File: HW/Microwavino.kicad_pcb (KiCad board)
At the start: 2 copper layers, 57 parts, among them P1 SMA, P2 SMA, P3 SMA, P4 SMA, U1 MIC5366, U2 MCP1824T, U3 MCP1824T, U4 MCP1824T, U5 ASTXR-12-19.200MHz, U6 MAX2871, U7 Teensy3.2

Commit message: prelim layout
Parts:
- removed C27, C29, C30: 1n, VNA:C_0603b
- removed P2, P3, P4: SMA, VNA:CONSMA003.062
- removed R10: 49.9, VNA:R_0402b
- added R13: DNP, VNA:R_0402b, F.Cu at (219.7, 79.4)
- added R14: DNP, VNA:R_0402b, F.Cu at (227.5, 79.4)
- C26: footprint VNA:C_0603b -> VNA:C_0402b
- U1: footprint VNA:SOT-23-5L -> VNA:SOT-23-5
- moved U7 100.8 mm to (89.5, 69.8), turned to 270 degrees
- moved C28 58.6 mm to (171.3, 76.2)
- moved R9 58.6 mm to (169.4, 75.6)
- moved R11 54.2 mm to (151.8, 75.6)
- moved C25 50.6 mm to (138.3, 76.2)
- moved R6 50.6 mm to (136.4, 75.6)
- moved R7 50.6 mm to (136.4, 76.8)
- moved P1 23.2 mm to (89.7, 85.5)
- moved C26 19.8 mm to (89.7, 81.5)
- moved R8 19.0 mm to (91.4, 80.7), turned to 180 degrees
- moved C1 11.4 mm to (85.7, 59.4), turned to 180 degrees
- moved U1 8.87 mm to (86.6, 60.8), turned to 180 degrees
- moved C5 3.16 mm to (85.7, 65.0), turned to 180 degrees
- moved R3 1.94 mm to (83.4, 75.6), turned to 270 degrees
- moved R12 1.45 mm to (85.5, 72.9), turned to 0 degrees
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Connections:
- FB3 pad 2: Net-(FB3-Pad2) -> /3V3_PLL
- U7 pad 6: CE -> LE
- U7 pad 7: LE -> CE
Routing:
- net Net-(C24-Pad1): track 0.00 -> 16.6 mm, vias 0 -> 2
- net DATA: track 0.00 -> 14.9 mm, vias 0 -> 1
- net RFOUT_EN: track 0.00 -> 12.4 mm, vias 0 -> 1
- net LE: track 0.00 -> 11.6 mm
- net CE: track 0.00 -> 10.1 mm
- net MUXOUT: track 0.00 -> 9.60 mm, vias 0 -> 1
- net Net-(R3-Pad2): track 0.00 -> 7.42 mm, vias 0 -> 2
- net /3V3_PLL: track 0.00 -> 5.86 mm
- net /3V3_DIG: track 0.00 -> 5.81 mm
- net /3V3_VCO: track 0.00 -> 5.29 mm
- net /RF_OUTA_P: track 0.00 -> 4.37 mm
- net Net-(C12-Pad1): track 0.00 -> 3.36 mm
- net Net-(C26-Pad1): track 0.00 -> 3.27 mm
- net /RF_OUTB_N: track 0.00 -> 3.11 mm
- net Net-(C9-Pad1): track 0.00 -> 2.91 mm
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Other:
- board outline added: 17.8 x 35.6 mm
- net class Default: clearance 0.2 -> 0.1524; via_dia 0.6 -> 0.554; via_drill 0.4 -> 0.3
- net class PWR: clearance 0.1 -> 0.1524; via_dia 0.4 -> 0.554
- net class RF: clearance 0.1 -> 0.2; trace_width 0.75 -> 0.85; via_dia 0.4 -> 0.554
- net class SPI: clearance 0.1 -> 0.1524; via_dia 0.4 -> 0.554
- rule trace_clearance: 0.2 -> 0.1524

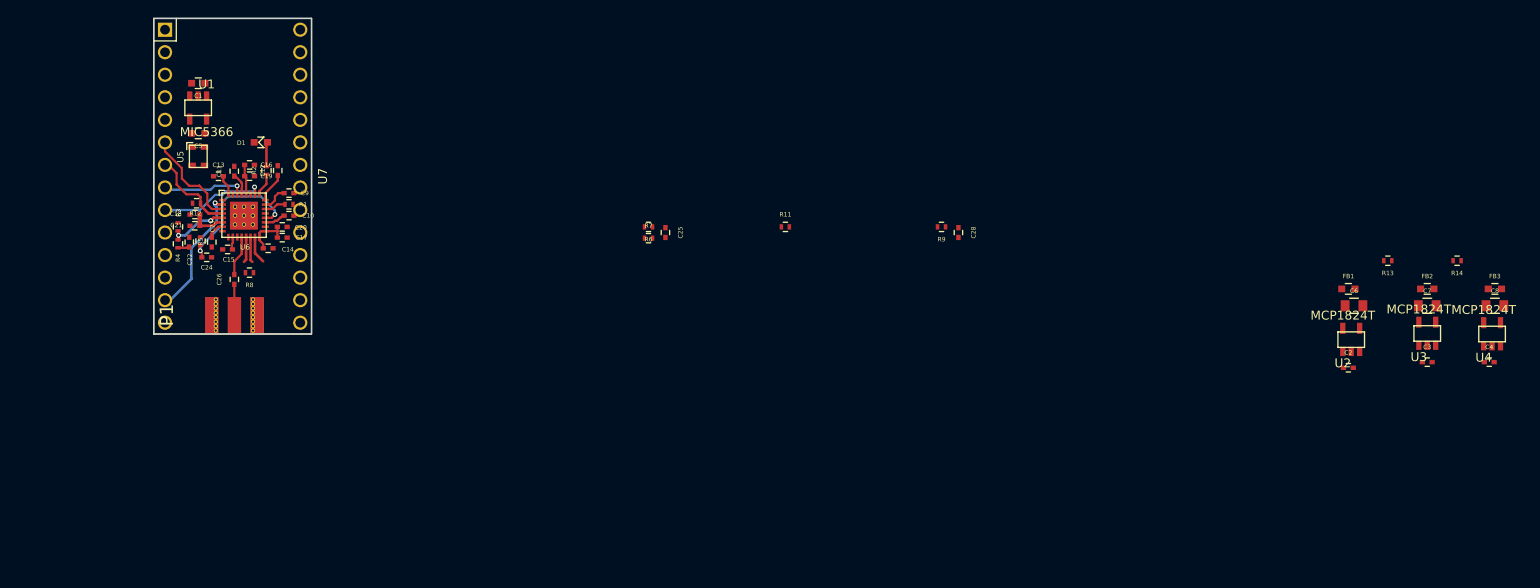
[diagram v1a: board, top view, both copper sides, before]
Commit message: route all except power
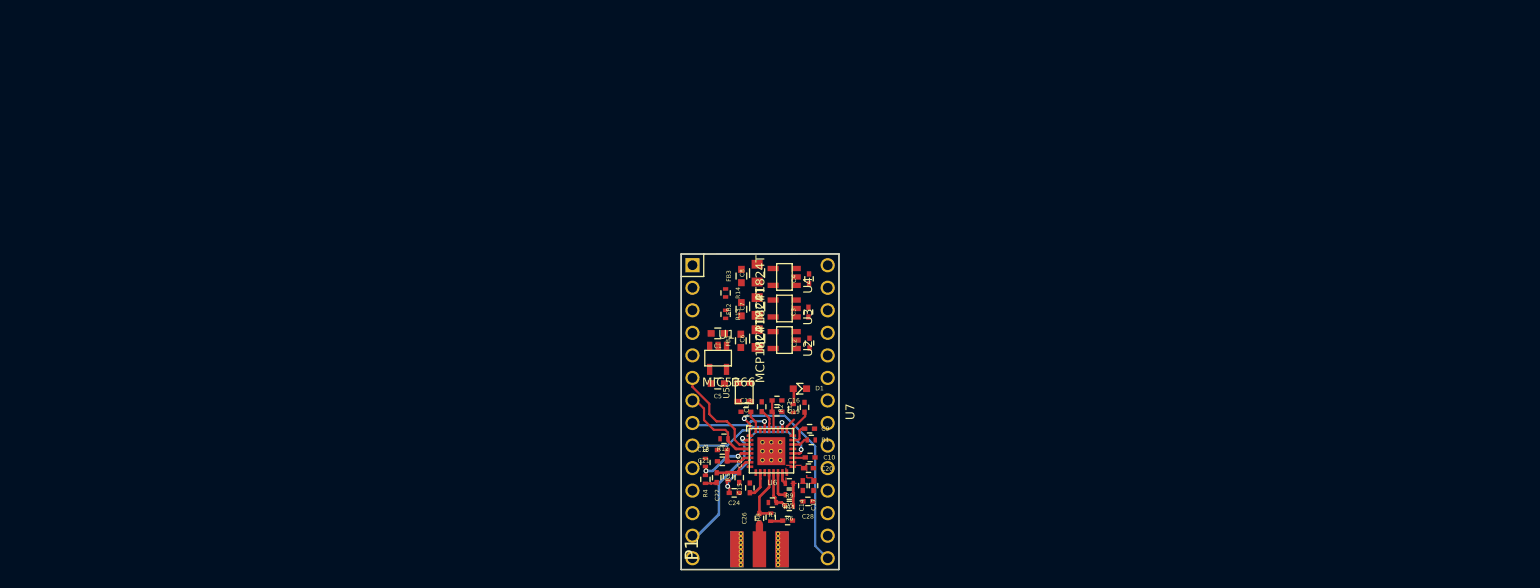
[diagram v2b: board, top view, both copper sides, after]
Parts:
- moved FB3 84.9 mm to (146.9, 81.1), turned to 90 degrees
- moved C8 83.2 mm to (148.6, 80.8), turned to 90 degrees
- moved R14 82.5 mm to (145.1, 83.0), turned to 270 degrees
- moved U4 79.1 mm to (151.8, 81.2), turned to 180 degrees
- moved FB2 77.3 mm to (146.9, 84.8), turned to 90 degrees
- moved C4 77.2 mm to (154.5, 81.4), turned to 90 degrees
- moved C7 75.5 mm to (148.7, 84.5), turned to 90 degrees
- moved R13 74.9 mm to (145.1, 85.4), turned to 270 degrees
- moved U3 71.6 mm to (151.8, 84.7), turned to 180 degrees
- moved C3 70.0 mm to (154.4, 85.2), turned to 90 degrees
- moved FB1 68.7 mm to (146.8, 88.4), turned to 90 degrees
- moved C6 67.4 mm to (148.7, 88.1), turned to 90 degrees
- moved U5 67.0 mm to (147.2, 94.2)
- moved D1 66.8 mm to (153.5, 93.8), turned to 180 degrees
- moved C17 66.1 mm to (155.0, 104.7), turned to 270 degrees
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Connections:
- U7 pad 33: Net-(U7-Pad33) -> VCC
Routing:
- net CLK: track 0.00 -> 25.0 mm, vias 0 -> 1
- net Net-(C22-Pad2): track 2.05 -> 5.65 mm
- net /3V3_PLL: track 5.86 -> 8.18 mm
- net /RF_OUTA_P: track 4.37 -> 6.34 mm
- net /RF_OUTA_N: track 2.90 -> 4.67 mm
- net /RF_OUTB_N: track 3.11 -> 1.35 mm
- net /3V3_VCO: track 5.29 -> 3.92 mm
- net Net-(D1-Pad2): track 2.77 -> 1.54 mm
- net LD: track 2.54 -> 1.47 mm
- net Net-(C10-Pad1): track 2.43 -> 1.42 mm
- net Net-(R1-Pad1): track 2.43 -> 1.92 mm
- added copper zone on F.Cu, net /3V3_VCO

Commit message: layout completed v1.0
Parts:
- added REF**: Via_0.3_0.6, VNA:Via_0.3_0.6, F.Cu at (147.8, 109.3)
- added REF**: Via_0.3_0.6, VNA:Via_0.3_0.6, F.Cu at (144.2, 90.8)
- added REF**: Via_0.3_0.6, VNA:Via_0.3_0.6, F.Cu at (144.3, 89.0)
- added REF**: Via_0.3_0.6, VNA:Via_0.3_0.6, F.Cu at (144.5, 101.5)
- added REF**: Via_0.3_0.6, VNA:Via_0.3_0.6, F.Cu at (142.9, 100.2)
- added REF**: Via_0.3_0.6, VNA:Via_0.3_0.6, F.Cu at (148.2, 103.8)
- added REF**: Via_0.3_0.6, VNA:Via_0.3_0.6, F.Cu at (147.6, 106.2)
- added REF**: Via_0.3_0.6, VNA:Via_0.3_0.6, F.Cu at (146.7, 106.6)
- added REF**: Via_0.3_0.6, VNA:Via_0.3_0.6, F.Cu at (149.9, 106.1)
- added REF**: Via_0.3_0.6, VNA:Via_0.3_0.6, F.Cu at (152.6, 109.5)
- added REF**: Via_0.3_0.6, VNA:Via_0.3_0.6, F.Cu at (152.4, 90.6)
- added REF**: Via_0.3_0.6, VNA:Via_0.3_0.6, F.Cu at (148.1, 106.7)
- added REF**: Via_0.3_0.6, VNA:Via_0.3_0.6, F.Cu at (151.8, 88.3)
- added REF**: Via_0.3_0.6, VNA:Via_0.3_0.6, F.Cu at (151.8, 81.2)
- added REF**: Via_0.3_0.6, VNA:Via_0.3_0.6, F.Cu at (151.8, 84.8)
- added REF**: Via_0.3_0.6, VNA:Via_0.3_0.6, F.Cu at (151.8, 83.2)
- added REF**: Via_0.3_0.6, VNA:Via_0.3_0.6, F.Cu at (151.8, 86.5)
- added REF**: Via_0.3_0.6, VNA:Via_0.3_0.6, F.Cu at (143.9, 80.5)
- added REF**: Via_0.3_0.6, VNA:Via_0.3_0.6, F.Cu at (143.6, 86.1)
- added REF**: Via_0.3_0.6, VNA:Via_0.3_0.6, F.Cu at (148.1, 107.4)
- added REF**: Via_0.3_0.6, VNA:Via_0.3_0.6, F.Cu at (148.1, 108.4)
- added REF**: Via_0.3_0.6, VNA:Via_0.3_0.6, F.Cu at (149.9, 109.3)
- added REF**: Via_0.3_0.6, VNA:Via_0.3_0.6, F.Cu at (150.2, 107.4)
- added REF**: Via_0.3_0.6, VNA:Via_0.3_0.6, F.Cu at (145.9, 96.4)
- added REF**: Via_0.3_0.6, VNA:Via_0.3_0.6, F.Cu at (145.5, 95.2)
- added REF**: Via_0.3_0.6, VNA:Via_0.3_0.6, F.Cu at (143.4, 94.2)
- moved C15 0.81 mm to (148.4, 104.4), turned to 180 degrees
- moved C25 0.60 mm to (152.6, 108.3)
- moved R12 0.52 mm to (144.8, 98.9)
- moved R8 0.32 mm to (150.5, 108.3), turned to 180 degrees
- moved C24 0.09 mm to (146.1, 105.6)
- turned C28 to 0 degrees
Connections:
- D1 pad 2: Net-(D1-Pad2) -> LD
- R12 pad 1: /3V3_DIG -> /3V3_PLL
- R2 pad 1: LD -> Net-(R2-Pad1)
- R2 pad 2: Net-(D1-Pad2) -> LD
- U6 pad 25: LD -> Net-(R2-Pad1)
- U7 pad 10: LD -> Net-(U7-Pad10)
- U7 pad 28: Net-(U7-Pad28) -> LD
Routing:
- net GND: track 0.00 -> 42.2 mm
- net /3V3_PLL: track 8.18 -> 39.6 mm, vias 0 -> 4
- net /3V3_VCO: track 3.92 -> 33.0 mm, vias 0 -> 2
- net /3V3_DIG: track 5.81 -> 19.5 mm, vias 0 -> 3
- net /3V3_IN: track 0.00 -> 12.4 mm
- net Net-(C7-Pad1): track 0.00 -> 7.23 mm
- net /1V8: track 0.00 -> 5.43 mm
- net LD: track 1.47 -> 6.38 mm
- net Net-(C8-Pad1): track 0.00 -> 3.62 mm
- net Net-(R2-Pad1): track 0.00 -> 2.47 mm
- net Net-(D1-Pad2): track 1.54 -> 0.00 mm
- net /CLK_REF: track 0.00 -> 1.28 mm
- net DATA: track 14.9 -> 16.1 mm
- net Net-(R3-Pad2): track 7.42 -> 8.49 mm
- net CE: track 10.1 -> 11.1 mm
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- added copper zone on B.Cu, net GND
- added copper zone on F.Cu, net GND
- added copper zone on F.Cu, net VCC
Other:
- board text added: "More things I hate about Kicad: - When I set Front layer to invisible, I want to hide all of Front layer, and not leave pads visible! - When I reroute the trace, I want old trace deleted every time, not leave it standing there as it was or delete it only sometimes. - For via stitching I need to create component pads - Duplicate component works only in F11 view"

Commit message: drc pass
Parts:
- removed the REF** at (147.8, 109.3)
- removed the REF** at (144.2, 90.8)
- removed the REF** at (144.3, 89.0)
- removed the REF** at (144.5, 101.5)
- removed the REF** at (142.9, 100.2)
- removed the REF** at (148.2, 103.8)
- removed the REF** at (147.6, 106.2)
- removed the REF** at (146.7, 106.6)
- removed the REF** at (149.9, 106.1)
- removed the REF** at (152.6, 109.5)
- removed the REF** at (152.4, 90.6)
- removed the REF** at (148.1, 106.7)
- removed the REF** at (151.8, 88.3)
- removed the REF** at (151.8, 81.2)
- removed the REF** at (151.8, 83.2)
- removed the REF** at (151.8, 86.5)
- removed the REF** at (143.9, 80.5)
- removed the REF** at (143.6, 86.1)
- removed the REF** at (148.1, 107.4)
- removed the REF** at (148.1, 108.4)
- removed the REF** at (150.2, 107.4)
- removed the REF** at (145.9, 96.4)
- removed the REF** at (145.5, 95.2)
- removed the REF** at (143.4, 94.2)
- added REF**: Via_0.3_0.6, VNA:Via_0.3_0.6, F.Cu at (144.2, 91.6)
- added REF**: Via_0.3_0.6, VNA:Via_0.3_0.6, F.Cu at (154.7, 112.2)
- added REF**: Via_0.3_0.6, VNA:Via_0.3_0.6, F.Cu at (154.4, 108.2)
- added REF**: Via_0.3_0.6, VNA:Via_0.3_0.6, F.Cu at (154.4, 109.5)
- added REF**: Via_0.3_0.6, VNA:Via_0.3_0.6, F.Cu at (155.2, 110.3)
- added REF**: Via_0.3_0.6, VNA:Via_0.3_0.6, F.Cu at (155.1, 113.4)
- added REF**: Via_0.3_0.6, VNA:Via_0.3_0.6, F.Cu at (155.1, 97.7)
- added REF**: Via_0.3_0.6, VNA:Via_0.3_0.6, F.Cu at (154.9, 107.2)
- added REF**: Via_0.3_0.6, VNA:Via_0.3_0.6, F.Cu at (155.7, 106.5)
- added REF**: Via_0.3_0.6, VNA:Via_0.3_0.6, F.Cu at (144.1, 108.5)
- added REF**: Via_0.3_0.6, VNA:Via_0.3_0.6, F.Cu at (144.1, 111.4)
- added REF**: Via_0.3_0.6, VNA:Via_0.3_0.6, F.Cu at (152.9, 113.5)
- added REF**: Via_0.3_0.6, VNA:Via_0.3_0.6, F.Cu at (145.3, 113.4)
- added REF**: Via_0.3_0.6, VNA:Via_0.3_0.6, F.Cu at (144.1, 113.4)
- added REF**: Via_0.3_0.6, VNA:Via_0.3_0.6, F.Cu at (142.9, 113.4)
- added REF**: Via_0.3_0.6, VNA:Via_0.3_0.6, F.Cu at (144.2, 105.5)
- added REF**: Via_0.3_0.6, VNA:Via_0.3_0.6, F.Cu at (142.5, 98.7)
- added REF**: Via_0.3_0.6, VNA:Via_0.3_0.6, F.Cu at (142.9, 100.2)
- added REF**: Via_0.3_0.6, VNA:Via_0.3_0.6, F.Cu at (151.1, 107.5)
- added REF**: Via_0.3_0.6, VNA:Via_0.3_0.6, F.Cu at (151.5, 109.2)
- added REF**: Via_0.3_0.6, VNA:Via_0.3_0.6, F.Cu at (147.9, 109.3)
- added REF**: Via_0.3_0.6, VNA:Via_0.3_0.6, F.Cu at (155.6, 91.2)
- added REF**: Via_0.3_0.6, VNA:Via_0.3_0.6, F.Cu at (148.1, 108.4)
- added REF**: Via_0.3_0.6, VNA:Via_0.3_0.6, F.Cu at (148.2, 107.2)
- added REF**: Via_0.3_0.6, VNA:Via_0.3_0.6, F.Cu at (148.2, 106.2)
- added REF**: Via_0.3_0.6, VNA:Via_0.3_0.6, F.Cu at (147.8, 103.1)
- added REF**: Via_0.3_0.6, VNA:Via_0.3_0.6, F.Cu at (147.8, 103.8)
- added REF**: Via_0.3_0.6, VNA:Via_0.3_0.6, F.Cu at (147.2, 104.4)
- added REF**: Via_0.3_0.6, VNA:Via_0.3_0.6, F.Cu at (146.7, 106.2)
- added REF**: Via_0.3_0.6, VNA:Via_0.3_0.6, F.Cu at (146.2, 98.4)
- added REF**: Via_0.3_0.6, VNA:Via_0.3_0.6, F.Cu at (143.9, 102.4)
- added REF**: Via_0.3_0.6, VNA:Via_0.3_0.6, F.Cu at (145.6, 95.2)
- added REF**: Via_0.3_0.6, VNA:Via_0.3_0.6, F.Cu at (145.9, 84.3)
- added REF**: Via_0.3_0.6, VNA:Via_0.3_0.6, F.Cu at (143.5, 94.3)
- added REF**: Via_0.3_0.6, VNA:Via_0.3_0.6, F.Cu at (143.8, 86.2)
- added REF**: Via_0.3_0.6, VNA:Via_0.3_0.6, F.Cu at (143.8, 84.5)
- added REF**: Via_0.3_0.6, VNA:Via_0.3_0.6, F.Cu at (144.4, 81.0)
- added REF**: Via_0.3_0.6, VNA:Via_0.3_0.6, F.Cu at (142.9, 82.4)
- added REF**: Via_0.3_0.6, VNA:Via_0.3_0.6, F.Cu at (145.9, 79.4)
- added REF**: Via_0.3_0.6, VNA:Via_0.3_0.6, F.Cu at (151.2, 79.3)
- added REF**: Via_0.3_0.6, VNA:Via_0.3_0.6, F.Cu at (152.1, 90.1)
- added REF**: Via_0.3_0.6, VNA:Via_0.3_0.6, F.Cu at (151.8, 88.3)
- added REF**: Via_0.3_0.6, VNA:Via_0.3_0.6, F.Cu at (151.8, 86.6)
- added REF**: Via_0.3_0.6, VNA:Via_0.3_0.6, F.Cu at (146.0, 82.6)
- added REF**: Via_0.3_0.6, VNA:Via_0.3_0.6, F.Cu at (151.8, 83.1)
- added REF**: Via_0.3_0.6, VNA:Via_0.3_0.6, F.Cu at (151.8, 81.2)
- added REF**: Via_0.3_0.6, VNA:Via_0.3_0.6, F.Cu at (154.8, 95.4)
- added REF**: Via_0.3_0.6, VNA:Via_0.3_0.6, F.Cu at (155.1, 93.9)
- added REF**: Via_0.3_0.6, VNA:Via_0.3_0.6, F.Cu at (152.8, 109.1)
- added REF**: Via_0.3_0.6, VNA:Via_0.3_0.6, F.Cu at (149.9, 107.2)
- added REF**: Via_0.3_0.6, VNA:Via_0.3_0.6, F.Cu at (145.9, 96.4)
- added REF**: Via_0.3_0.6, VNA:Via_0.3_0.6, F.Cu at (146.5, 94.4)
- added REF**: Via_0.3_0.6, VNA:Via_0.3_0.6, F.Cu at (152.8, 110.3)
- added REF**: Via_0.3_0.6, VNA:Via_0.3_0.6, F.Cu at (153.7, 111.1)
- moved R12 0.29 mm to (144.5, 98.9)
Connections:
- U7 pad 10: Net-(U7-Pad10) -> GND
- U7 pad 11: Net-(U7-Pad11) -> GND
- U7 pad 14: Net-(U7-Pad14) -> MUXOUT
- U7 pad 23: Net-(U7-Pad23) -> GND
- U7 pad 24: Net-(U7-Pad24) -> GND
- U7 pad 8: MUXOUT -> RFOUT_EN
- U7 pad 9: RFOUT_EN -> Net-(U7-Pad9)
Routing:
- net MUXOUT: track 9.60 -> 20.6 mm
- net Net-(C8-Pad1): track 3.62 -> 5.42 mm
- net /3V3_PLL: track 39.6 -> 40.9 mm
- net CE: track 11.1 -> 10.5 mm
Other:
- board text added: "More things I hate about Kicad: - When I set Front layer to invisible, I want to hide all of Front layer, and not leave pads visible! - When I reroute the trace, I want old trace deleted every time, not leave it standing there as it was or delete it only sometimes. - For via stitching I need to create component pads - and then, reading new netlist kills those pads - Duplicate component works only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"
- board text removed: "More things I hate about Kicad: - When I set Front layer to invisible, I want to hide all of Front layer, and not leave pads visible! - When I reroute the trace, I want old trace deleted every time, not leave it standing there as it was or delete it only sometimes. - For via stitching I need to create component pads - Duplicate component works only in F11 view"

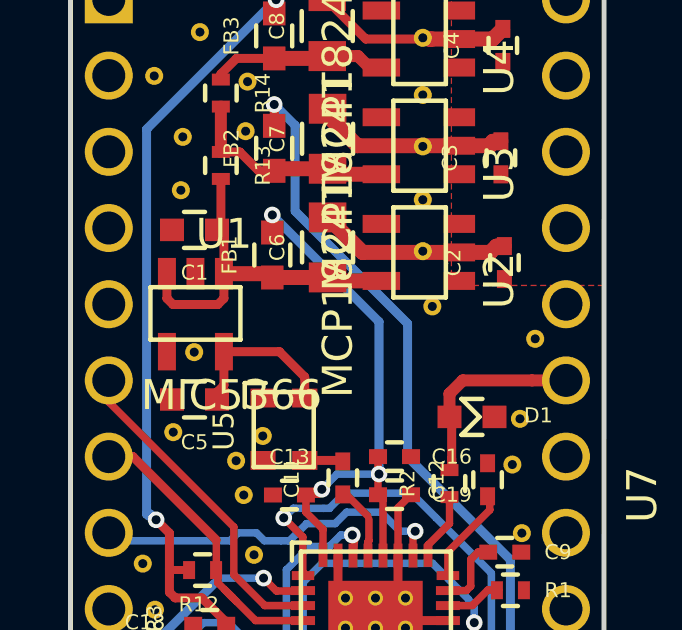
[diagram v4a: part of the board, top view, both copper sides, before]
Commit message: added footprint SOT-323-70-sc-5
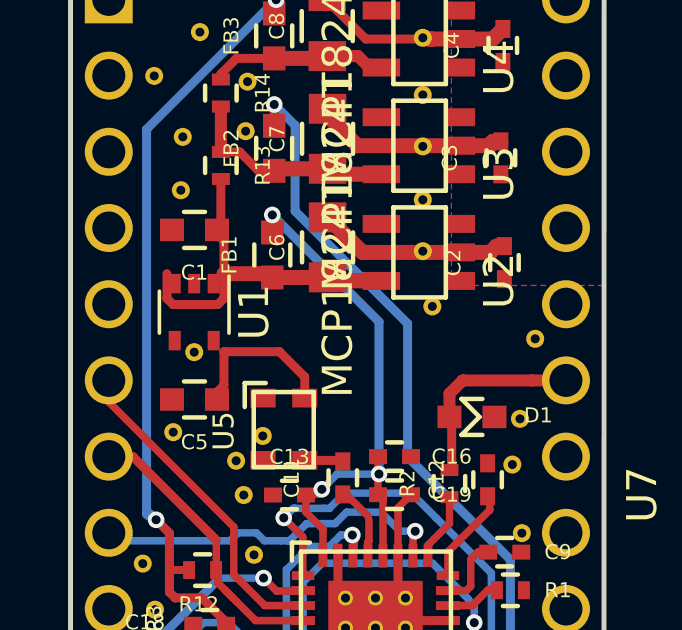
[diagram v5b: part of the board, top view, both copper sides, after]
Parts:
- U1: footprint VNA:SOT-23-5 -> VNA:SOT-353_SC-70-5
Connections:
- U2 pad 4: Net-(U2-Pad4) -> (no net)
- U3 pad 4: Net-(U3-Pad4) -> (no net)
- U4 pad 4: Net-(U4-Pad4) -> (no net)
- U7 pad 12: Net-(U7-Pad12) -> (no net)
- U7 pad 2: Net-(U7-Pad2) -> (no net)
- U7 pad 21: Net-(U7-Pad21) -> (no net)
- U7 pad 22: Net-(U7-Pad22) -> (no net)
- U7 pad 25: Net-(U7-Pad25) -> (no net)
- U7 pad 26: Net-(U7-Pad26) -> (no net)
- U7 pad 27: Net-(U7-Pad27) -> (no net)
- U7 pad 29: Net-(U7-Pad29) -> (no net)
- U7 pad 3: Net-(U7-Pad3) -> (no net)
- U7 pad 30: Net-(U7-Pad30) -> (no net)
- U7 pad 31: Net-(U7-Pad31) -> (no net)
- U7 pad 32: Net-(U7-Pad32) -> (no net)
- U7 pad 4: Net-(U7-Pad4) -> (no net)
- U7 pad 5: Net-(U7-Pad5) -> (no net)
- U7 pad 9: Net-(U7-Pad9) -> (no net)

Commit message: released and ordered
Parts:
- added REF**: Via_0.3_0.6, VNA:Via_0.3_0.6, F.Cu at (149.8, 106.0)
- added REF**: Via_0.3_0.6, VNA:Via_0.3_0.6, F.Cu at (149.5, 94.2)
- added REF**: Via_0.3_0.6, VNA:Via_0.3_0.6, F.Cu at (152.1, 92.0)
- added REF**: Via_0.3_0.6, VNA:Via_0.3_0.6, F.Cu at (147.9, 91.1)
- added REF**: Via_0.3_0.6, VNA:Via_0.3_0.6, F.Cu at (149.4, 91.1)
- added REF**: Via_0.3_0.6, VNA:Via_0.3_0.6, F.Cu at (146.0, 90.4)
- moved REF** 0.25 mm to (144.2, 91.9)
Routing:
- net /1V8: track 5.43 -> 6.25 mm
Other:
- rule trace_min: 0.2 -> 0.25
- board text added: "Microwavino v1.0 Pero, 2017"
- board text added: "www.helentronica.com"
